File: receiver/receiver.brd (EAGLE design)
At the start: 88.9 x 88.9 mm, 41 parts, among them IC1 MAX3095CEE, IC2 MAX3095CEE

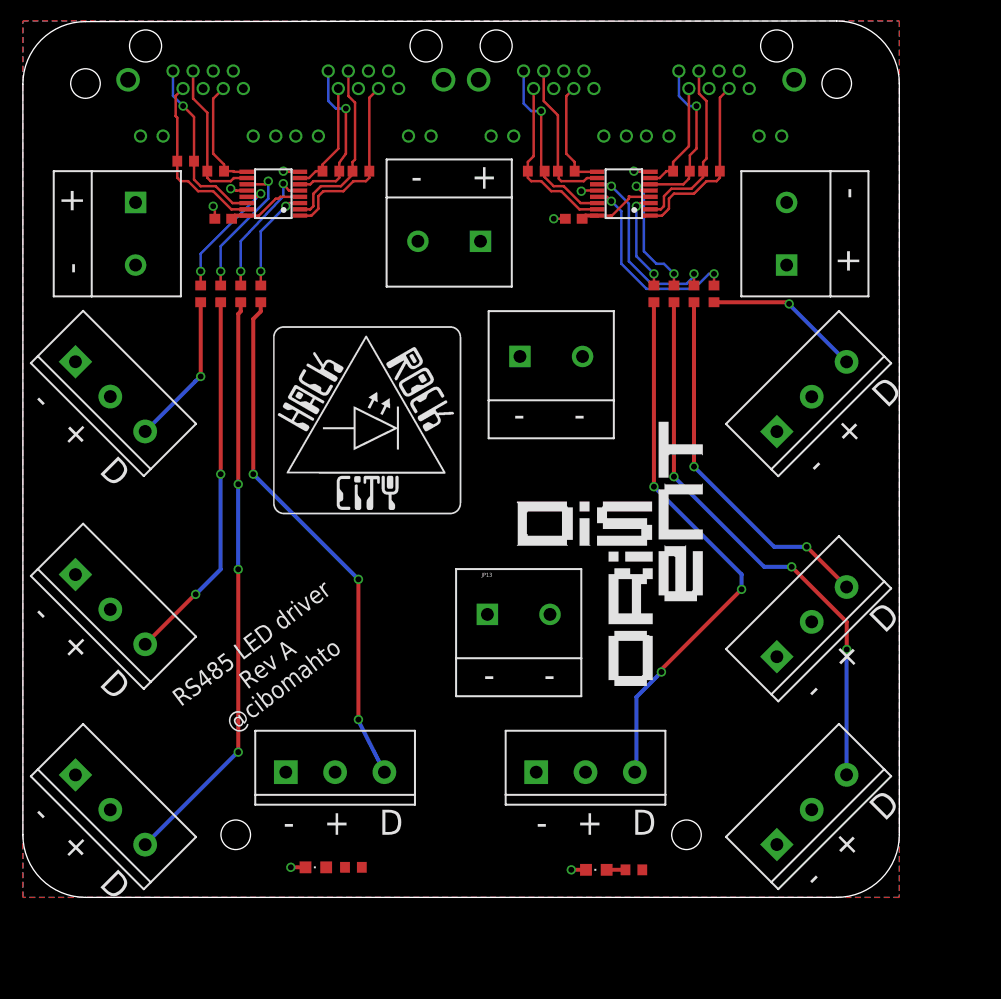
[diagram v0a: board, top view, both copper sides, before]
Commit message: Minor nits for receiver pcb order: fix text silkscreen, move outline to dimension layer and give it width
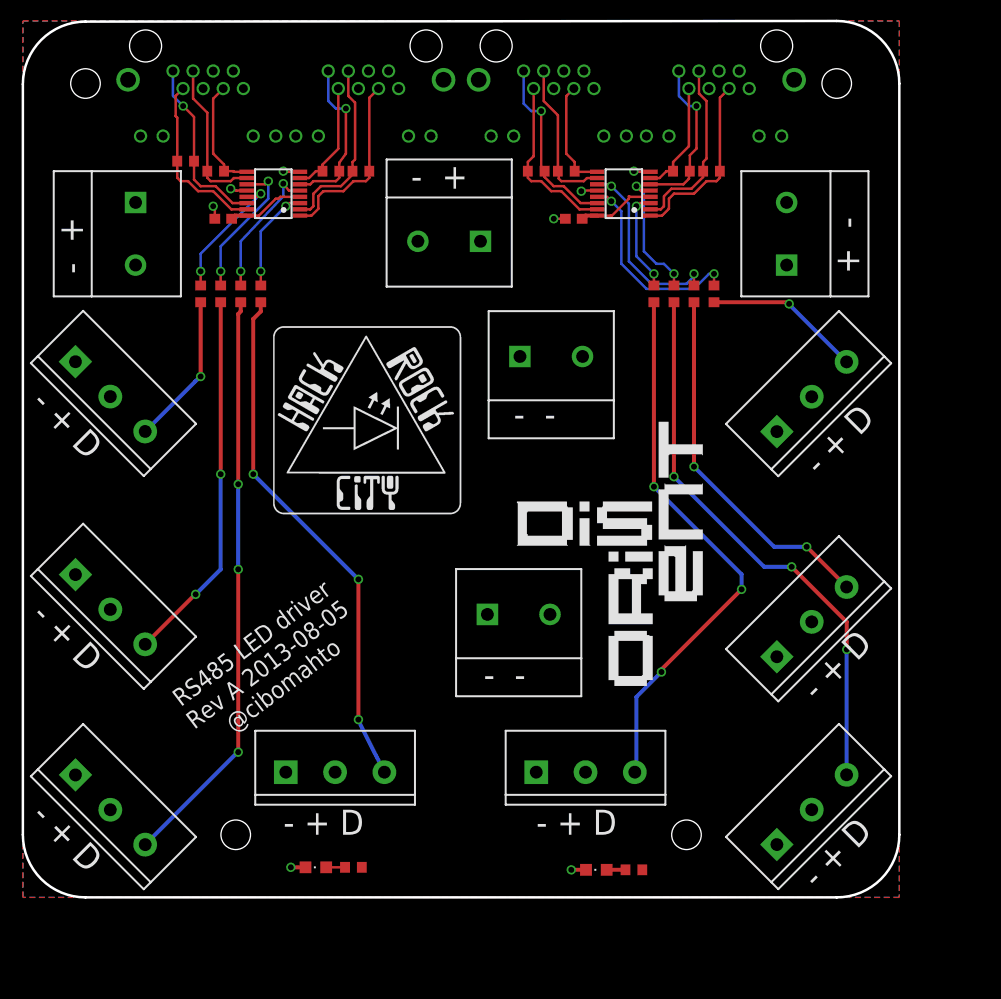
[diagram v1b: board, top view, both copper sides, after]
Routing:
- net N$27: track 0.00 -> 1.91 mm
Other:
- board text added: "RS485 LED driver Rev A 2013-08-05 @cibomahto"
- board text removed: "RS485 LED driver Rev A @cibomahto"
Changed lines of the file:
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@@
 <board>
 <plain>
-<wire x1="82.544571875" y1="88.894565625" x2="6.344571875" y2="88.829425" width="0" layer="20"/>
-<wire x1="6.344571875" y1="88.829425" x2="0" y2="82.479425" width="0" layer="20" curve="89.954797"/>
-<wire x1="0" y1="82.479425" x2="0" y2="6.35" width="0" layer="20"/>
-<wire x1="0" y1="6.35" x2="6.35" y2="0" width="0" layer="20" curve="90"/>
-<wire x1="6.35" y1="0" x2="82.55" y2="0" width="0" layer="20"/>
-<wire x1="82.55" y1="0" x2="88.9" y2="6.35" width="0" layer="20" curve="90"/>
-<wire x1="88.9" y1="6.35" x2="88.9" y2="82.54456875" width="0" layer="20"/>
-<wire x1="88.9" y1="82.54456875" x2="82.544571875" y2="88.894565625" width="0" layer="20" curve="90.048978"/>
+<wire x1="82.544571875" y1="88.894565625" x2="6.344571875" y2="88.829425" width="0.254" layer="20"/>
+<wire x1="6.344571875" y1="88.829425" x2="0" y2="82.479425" width="0.254" layer="20" curve="89.954797"/>
+<wire x1="0" y1="82.479425" x2="0" y2="6.35" width="0.254" layer="20"/>
+<wire x1="0" y1="6.35" x2="6.35" y2="0" width="0.254" layer="20" curve="90"/>
+<wire x1="6.35" y1="0" x2="82.55" y2="0" width="0.254" layer="20"/>
+<wire x1="82.55" y1="0" x2="88.9" y2="6.35" width="0.254" layer="20" curve="90"/>
+<wire x1="88.9" y1="6.35" x2="88.9" y2="82.54456875" width="0.254" layer="20"/>
+<wire x1="88.9" y1="82.54456875" x2="82.544571875" y2="88.894565625" width="0.254" layer="20" curve="90.048978"/>
 <hole x="6.35" y="82.55" drill="3"/>
 <hole x="21.59" y="6.35" drill="3"/>
 <hole x="67.31" y="6.35" drill="3"/>
 <hole x="82.55" y="82.55" drill="3"/>
-<text x="0.762" y="28.448" size="2.54" layer="25" rot="R315">-   +   D</text>
-<text x="0.762" y="8.128" size="2.54" layer="25" rot="R315">-   +   D</text>
-<text x="0.762" y="50.038" size="2.54" layer="25" rot="R315">-   +   D</text>
-<text x="26.416" y="6.35" size="2.54" layer="25">-   +   D</text>
-<text x="52.07" y="6.35" size="2.54" layer="25">-   +   D</text>
-<text x="80.518" y="0.762" size="2.54" layer="25" rot="R45">-   +   D</text>
-<text x="80.518" y="19.812" size="2.54" layer="25" rot="R45">-   +   D</text>
-<text x="80.772" y="42.672" size="2.54" layer="25" rot="R45">-   +   D</text>
-<text x="39.37" y="71.882" size="2.54" layer="25">-     +</text>
-<text x="84.836" y="63.246" size="2.54" layer="25" rot="R90">+     -</text>
-<text x="6.096" y="63.246" size="2.54" layer="25" rot="R90">-     +</text>
-<text x="49.784" y="47.752" size="2.54" layer="25">-     -</text>
-<text x="46.736" y="21.336" size="2.54" layer="25">-     -</text>
+<text x="0.762" y="28.448" size="2.54" layer="25" rot="R315">- + D</text>
+<text x="0.762" y="8.128" size="2.54" layer="25" rot="R315">- + D</text>
+<text x="0.762" y="50.038" size="2.54" layer="25" rot="R315">- + D</text>
+<text x="26.416" y="6.35" size="2.54" layer="25">- + D</text>
+<text x="52.07" y="6.35" size="2.54" layer="25">- + D</text>
+<text x="80.518" y="0.762" size="2.54" layer="25" rot="R45">- + D</text>
+<text x="80.518" y="19.812" size="2.54" layer="25" rot="R45">- + D</text>
+<text x="80.772" y="42.672" size="2.54" layer="25" rot="R45">- + D</text>
+<text x="39.37" y="71.882" size="2.54" layer="25">-  +</text>
+<text x="84.836" y="63.246" size="2.54" layer="25" rot="R90">+  -</text>
+<text x="6.096" y="63.246" size="2.54" layer="25" rot="R90">-  +</text>
+<text x="49.784" y="47.752" size="2.54" layer="25">-  -</text>
+<text x="46.736" y="21.336" size="2.54" layer="25">-  -</text>
 <text x="26.924" y="20.828" size="1.778" layer="25" rot="R37" align="bottom-center">RS485 LED driver
-Rev A
+Rev A 2013-08-05
 @cibomahto</text>
 <polygon width="0.4064" layer="41">
@@
 <element name="U$3" library="naim_misc" package="DISORIENT_LOGO" value="" x="61.468" y="35.306"/>
 <element name="U$4" library="naim_misc" package="HRC_LOGO_0.75IN" value="" x="25.4" y="38.862"/>
-<element name="JP13" library="SparkFun" package="SCREWTERMINAL-6.35MM-2" value="" x="50.292" y="28.702"/>
+<element name="JP13" library="SparkFun" package="SCREWTERMINAL-6.35MM-2" value="" x="50.292" y="28.702" smashed="yes">
+<attribute name="VALUE" x="46.522" y="31.242" size="0.4064" layer="27"/>
+</element>
 <element name="LED1" library="adafruit" package="CHIPLED_0805" value="" x="29.718" y="3.048" smashed="yes" rot="R90">
 <attribute name="VALUE" x="30.988" y="5.588" size="1.27" layer="27" rot="R180"/>
@@
 <contactref element="LED1" pad="A"/>
 <contactref element="R17" pad="1"/>
-<wire x1="32.678" y1="3.048" x2="30.768" y2="3.048" width="0" layer="19" extent="1-1"/>
+<wire x1="30.768" y1="3.048" x2="32.678" y2="3.048" width="0.254" layer="1"/>
 </signal>
 </signals>
